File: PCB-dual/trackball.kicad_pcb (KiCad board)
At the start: 2 copper layers, 48.8 x 42.5 mm, 8 parts, among them J3 Conn_01x01_Male, Q1 MMBT2222A-7-F, U1 Adafruit_QT_Py_M0, U2 MrJohnK_PMW3360DM-T2QU, U3 MrJohnK_PMW3360DM-T2QU

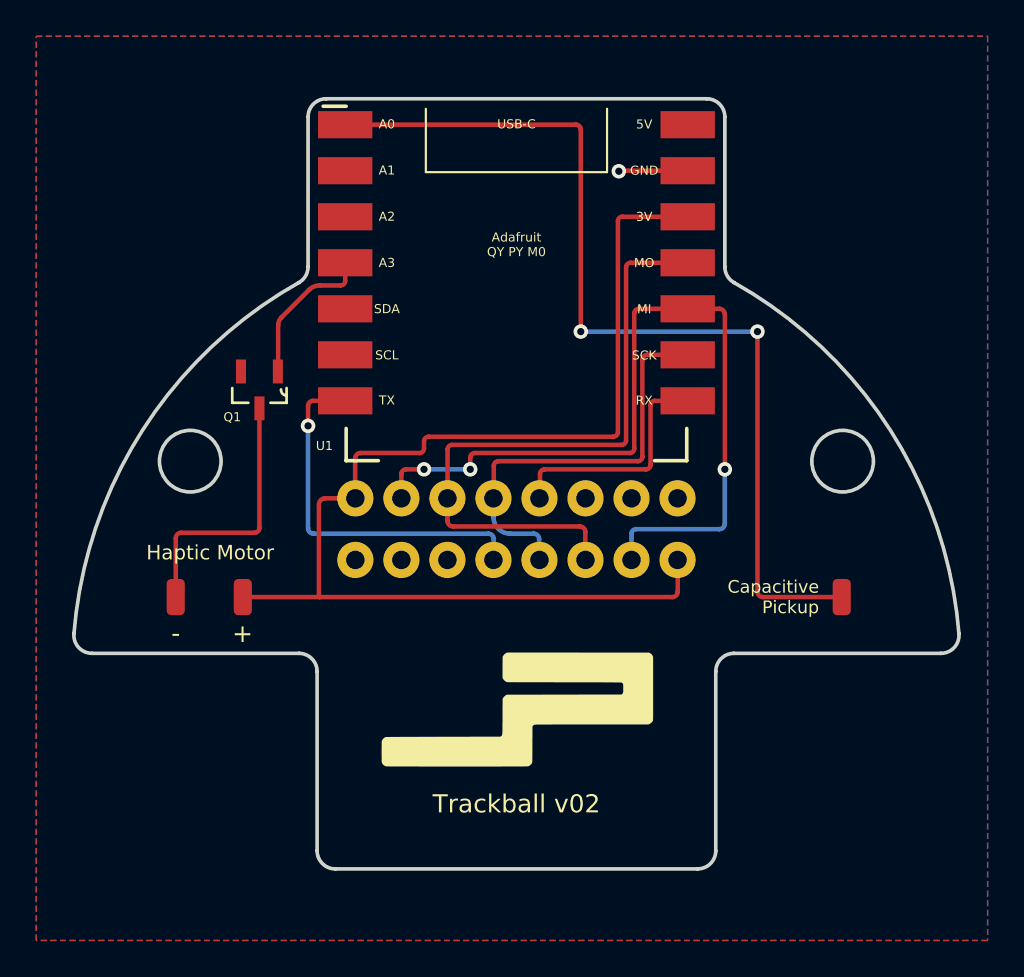
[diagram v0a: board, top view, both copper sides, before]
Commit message: feat: new v03 with new mounting hole placement and proper placement of second sensor with fitment in 55mm sphere sized case
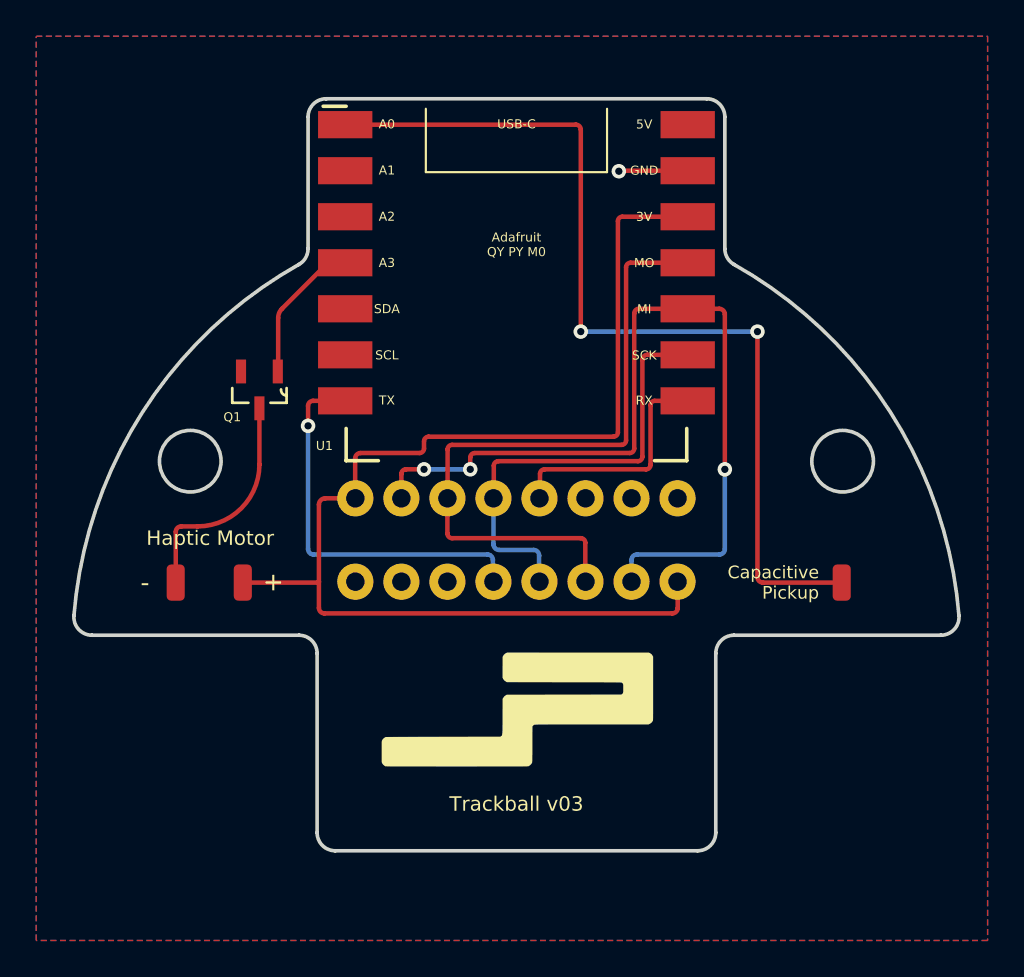
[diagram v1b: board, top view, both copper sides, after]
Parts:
- moved U3 1.20 mm to (144.5, 157.6)
- moved + 0.80 mm to (129.4, 148.7)
- moved - 0.80 mm to (125.7, 148.7)
- moved J3 0.80 mm to (162.4, 148.7)
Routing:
- net Net-(J2-Pad1): track 14.8 -> 12.5 mm
- net Net-(U1-Pad13): track 23.6 -> 25.1 mm
- net Net-(U1-Pad11): track 36.6 -> 37.9 mm
- net Net-(U1-Pad12): track 46.4 -> 47.6 mm
- net Net-(U1-Pad7): track 20.7 -> 21.8 mm
- net Net-(J3-Pad1): track 53.2 -> 52.4 mm
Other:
- board size 48.8 x 42.5 mm -> 48.8 x 41.5 mm
- board text added: "Trackball v03"
- board text removed: "Trackball v02"
